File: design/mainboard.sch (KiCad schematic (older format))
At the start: 0 parts

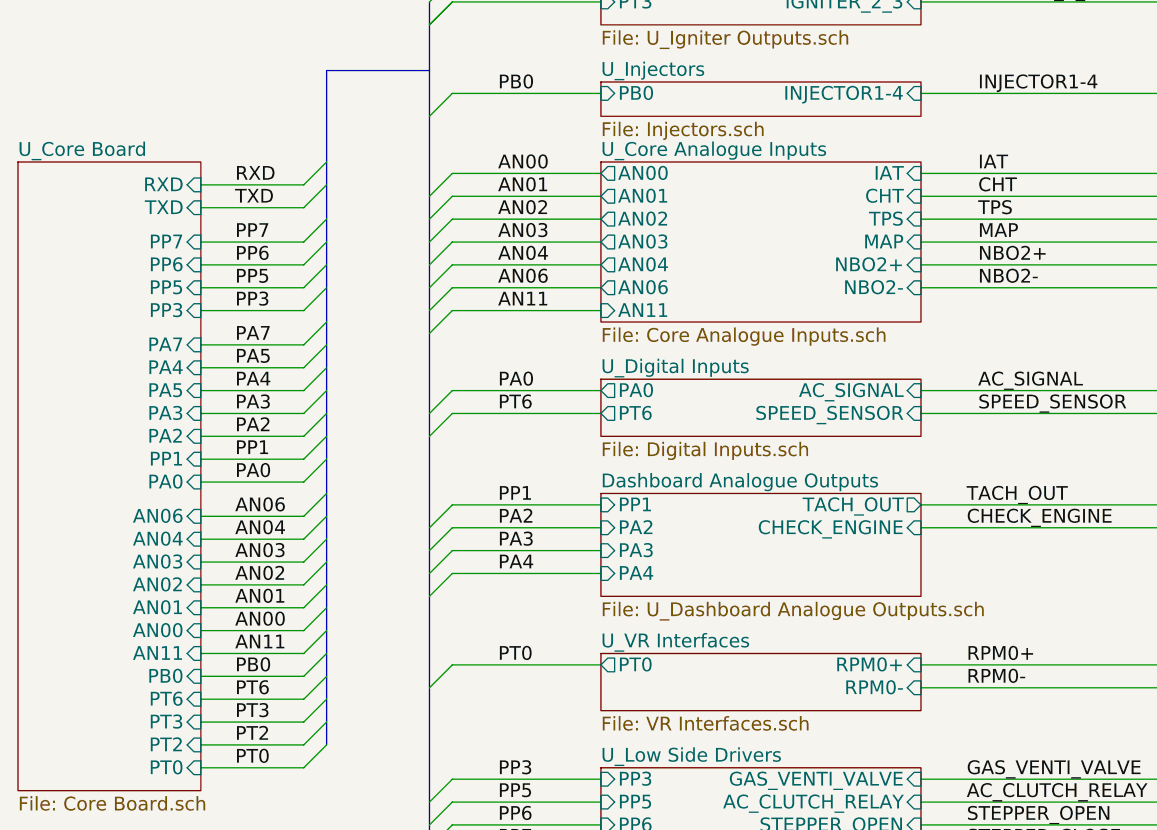
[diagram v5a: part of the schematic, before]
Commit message: make new footprint for max9924 & lm9040, add can bus interface, generate new netlist
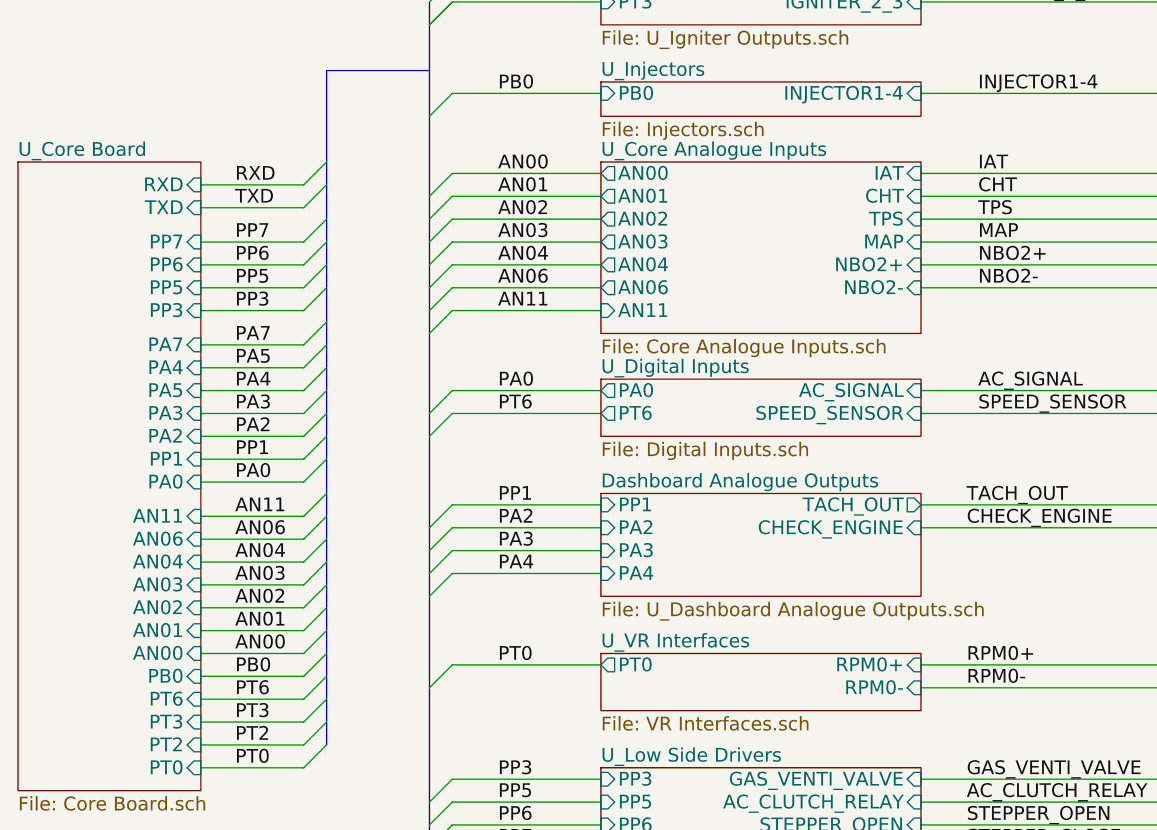
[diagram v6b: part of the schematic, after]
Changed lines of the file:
@@
-EESchema Schematic File Version 2  date 21/01/2012 01:12:26
+EESchema Schematic File Version 2  date 24/01/2012 16:34:51
 LIBS:power
 LIBS:device
@@
 Sheet 1 12
 Title "CatSquirt main board(code migrant worker)"
-Date "20 jan 2012"
+Date "24 jan 2012"
 Rev "0.01"
 Comp "diyefi.org"
@@
 Comment4 ""
 $EndDescr
-Text Label 2750 4500 0    60   ~ 0
+Text Label 2750 3900 0    60   ~ 0
 AN11
 Entry Wire Line
@@
 $EndSheet
 $Sheet
-S 4350 2350 1400 700
+S 4350 2350 1400 750
 U 4E918900
 F0 "U_Core Analogue Inputs" 60
@@
 F13 "PA2" I R 2600 3550 60
 F14 "PA0" I R 2600 3750 60
-F15 "AN04" I R 2600 4000 60
-F16 "AN03" I R 2600 4100 60
-F17 "AN02" I R 2600 4200 60
-F18 "AN01" I R 2600 4300 60
-F19 "AN00" I R 2600 4400 60
+F15 "AN04" I R 2600 4100 60
+F16 "AN03" I R 2600 4200 60
+F17 "AN02" I R 2600 4300 60
+F18 "AN01" I R 2600 4400 60
+F19 "AN00" I R 2600 4500 60
 F20 "PB0" I R 2600 4600 60
 F21 "PT3" I R 2600 4800 60
 F22 "PT2" I R 2600 4900 60
-F23 "AN06" I R 2600 3900 60
+F23 "AN06" I R 2600 4000 60
 F24 "PT6" I R 2600 4700 60
 F25 "PP1" I R 2600 3650 60
-F26 "AN11" I R 2600 4500 60
+F26 "AN11" I R 2600 3900 60
 $EndSheet
 $Sheet
@@
 Text Label 2750 4600 0    60   ~ 0
 PB0
+Text Label 2750 4500 0    60   ~ 0
+AN00
 Text Label 2750 4400 0    60   ~ 0
-AN00
+AN01
 Text Label 2750 4300 0    60   ~ 0
-AN01
+AN02
 Text Label 2750 4200 0    60   ~ 0
-AN02
+AN03
 Text Label 2750 4100 0    60   ~ 0
-AN03
+AN04
 Text Label 2750 4000 0    60   ~ 0
-AN04
-Text Label 2750 3900 0    60   ~ 0
 AN06
 Text Label 2750 3750 0    60   ~ 0
